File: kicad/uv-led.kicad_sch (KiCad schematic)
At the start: 11 parts, among them J1 JST_PH_B2B-PH-K_1x02_P2.00mm_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

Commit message: added screw specs to silkscreen (#3)
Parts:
- H1, H2: footprint MountingHole:MountingHole_3.2mm_M3_DIN965_Pad_TopOnly -> MountingHole:MountingHole_3.2mm_M3_ISO14580_Pad_TopOnly
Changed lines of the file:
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@@
 		)
 		(instances
-			(project "uv-led-pcb"
+			(project "uv-led"
 				(path "/e67fac83-14c9-457c-9fba-69cbeffeeea3"
 					(reference "#FLG03")
@@
 			)
 		)
-		(property "Footprint" "MountingHole:MountingHole_3.2mm_M3_DIN965_Pad_TopOnly"
+		(property "Footprint" "MountingHole:MountingHole_3.2mm_M3_ISO14580_Pad_TopOnly"
 			(at 152.4 102.87 0)
 			(hide yes)
@@
 		)
 		(instances
-			(project "uv-led-pcb"
+			(project "uv-led"
 				(path "/e67fac83-14c9-457c-9fba-69cbeffeeea3"
 					(reference "H1")
@@
 		)
 		(instances
-			(project "uv-led-pcb"
+			(project "uv-led"
 				(path "/e67fac83-14c9-457c-9fba-69cbeffeeea3"
 					(reference "D3")
@@
 		)
 		(instances
-			(project "uv-led-pcb"
+			(project "uv-led"
 				(path "/e67fac83-14c9-457c-9fba-69cbeffeeea3"
 					(reference "D2")
@@
 		)
 		(instances
-			(project "uv-led-pcb"
+			(project "uv-led"
 				(path "/e67fac83-14c9-457c-9fba-69cbeffeeea3"
 					(reference "D4")
@@
 		)
 		(instances
-			(project "uv-led-pcb"
+			(project "uv-led"
 				(path "/e67fac83-14c9-457c-9fba-69cbeffeeea3"
 					(reference "#PWR08")
@@
 		)
 		(instances
-			(project "uv-led-pcb"
+			(project "uv-led"
 				(path "/e67fac83-14c9-457c-9fba-69cbeffeeea3"
 					(reference "#PWR04")
@@
 		)
 		(instances
-			(project "uv-led-pcb"
+			(project "uv-led"
 				(path "/e67fac83-14c9-457c-9fba-69cbeffeeea3"
 					(reference "J1")
@@
 		)
 		(instances
-			(project "uv-led-pcb"
+			(project "uv-led"
 				(path "/e67fac83-14c9-457c-9fba-69cbeffeeea3"
 					(reference "#FLG04")
@@
 			)
 		)
-		(property "Footprint" "MountingHole:MountingHole_3.2mm_M3_DIN965_Pad_TopOnly"
+		(property "Footprint" "MountingHole:MountingHole_3.2mm_M3_ISO14580_Pad_TopOnly"
 			(at 177.8 102.87 0)
 			(hide yes)
@@
 		)
 		(instances
-			(project "uv-led-pcb"
+			(project "uv-led"
 				(path "/e67fac83-14c9-457c-9fba-69cbeffeeea3"
 					(reference "H2")
@@
 		)
 		(instances
-			(project "uv-led-pcb"
+			(project "uv-led"
 				(path "/e67fac83-14c9-457c-9fba-69cbeffeeea3"
 					(reference "D1")
@@
 		)
 		(instances
-			(project "uv-led-pcb"
+			(project "uv-led"
 				(path "/e67fac83-14c9-457c-9fba-69cbeffeeea3"
 					(reference "#PWR07")
@@
 		)
 		(instances
-			(project "uv-led-pcb"
+			(project "uv-led"
 				(path "/e67fac83-14c9-457c-9fba-69cbeffeeea3"
 					(reference "D5")
@@
 		)
 		(instances
-			(project "uv-led-pcb"
+			(project "uv-led"
 				(path "/e67fac83-14c9-457c-9fba-69cbeffeeea3"
 					(reference "#PWR02")
@@
 		)
 		(instances
-			(project "uv-led-pcb"
+			(project "uv-led"
 				(path "/e67fac83-14c9-457c-9fba-69cbeffeeea3"
 					(reference "#PWR03")
@@
 		)
 		(instances
-			(project "uv-led-pcb"
+			(project "uv-led"
 				(path "/e67fac83-14c9-457c-9fba-69cbeffeeea3"
 					(reference "H3")
@@
 		)
 		(instances
-			(project "uv-led-pcb"
+			(project "uv-led"
 				(path "/e67fac83-14c9-457c-9fba-69cbeffeeea3"
 					(reference "R1")
@@
 		)
 		(instances
-			(project "uv-led-pcb"
+			(project "uv-led"
 				(path "/e67fac83-14c9-457c-9fba-69cbeffeeea3"
 					(reference "H4")
@@
 		)
 		(instances
-			(project "uv-led-pcb"
+			(project "uv-led"
 				(path "/e67fac83-14c9-457c-9fba-69cbeffeeea3"
 					(reference "#PWR01")

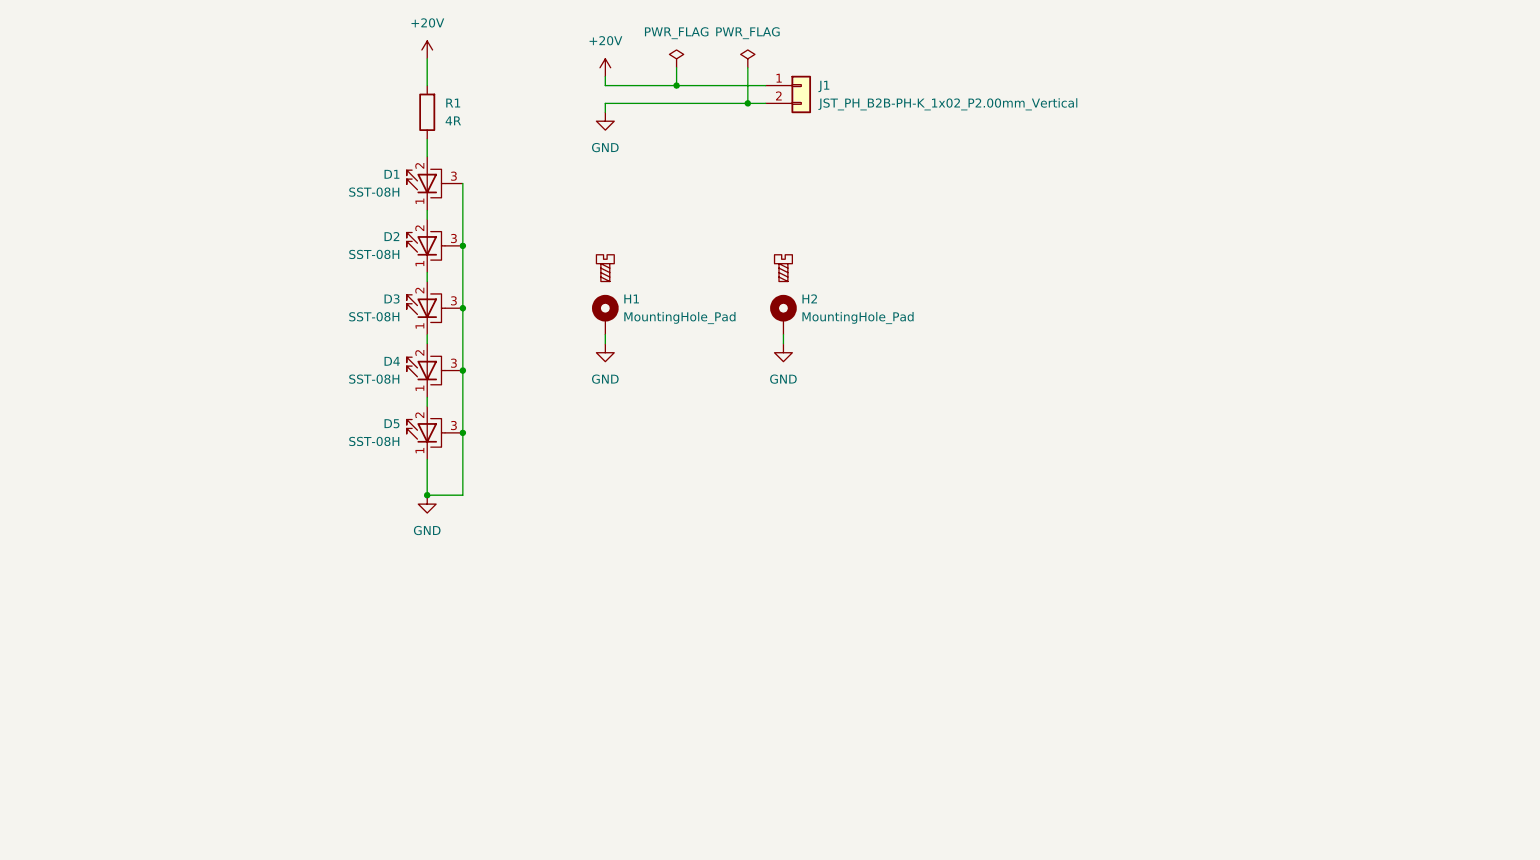
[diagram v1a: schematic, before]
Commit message: added design infos to PCB and schematic (#11)
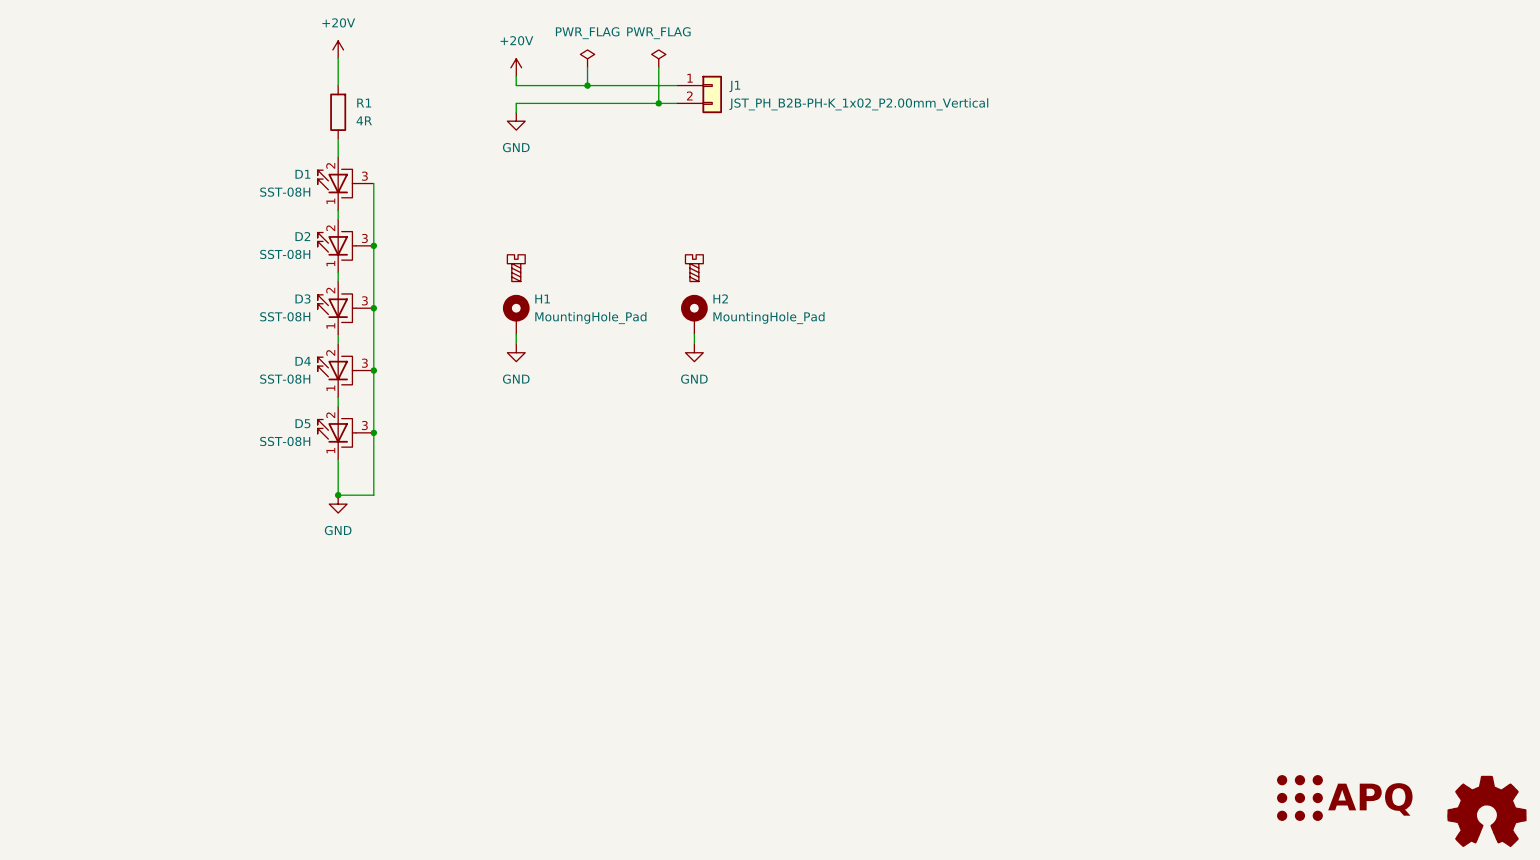
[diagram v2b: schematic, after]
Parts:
- added LOGO1: Logo_APQ, Custom_footprints_project:APQ-Logo_small, symbol Custom_logos:Logo_APQ
- added LOGO3: Logo_Open_Hardware_Small, Symbol:OSHW-Logo_7.5x8mm_SilkScreen, symbol Graphic:Logo_Open_Hardware_Small
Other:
- company: APQ - TU Darmstadt -> TU Darmstadt
- title: UV LED PCB -> QUIPS-C UV-LED
- moved on the sheet: D1, D2, D3, D4, D5, H1, H2, J1, R1

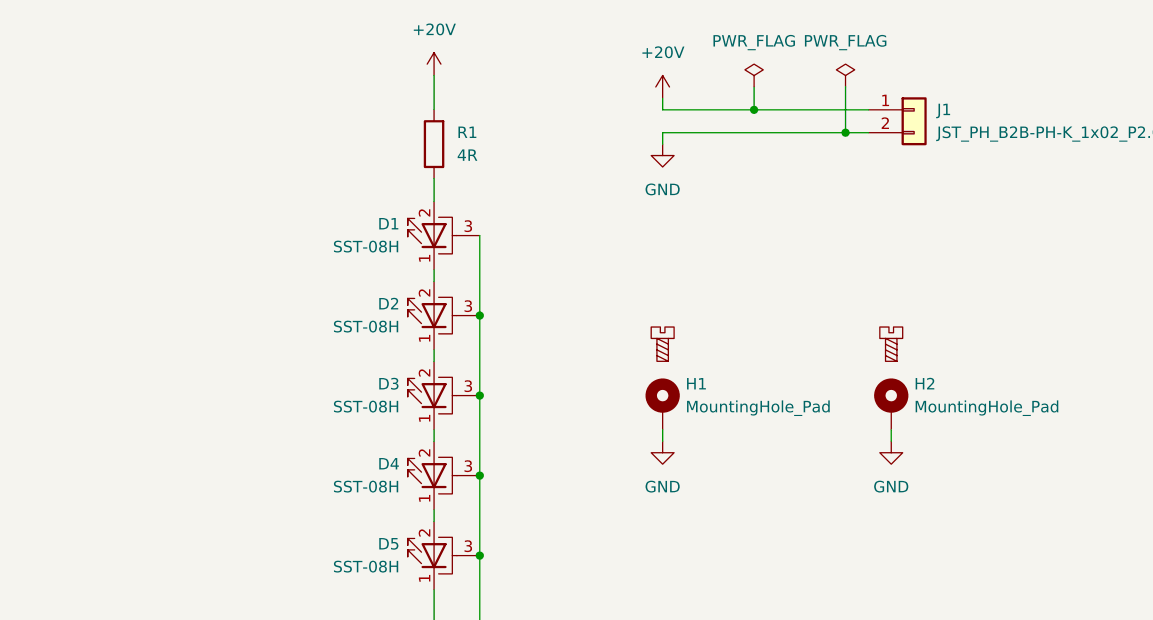
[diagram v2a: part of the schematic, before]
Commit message: added power and electrical details to schematic, updated silkscreen on PCB (#10)
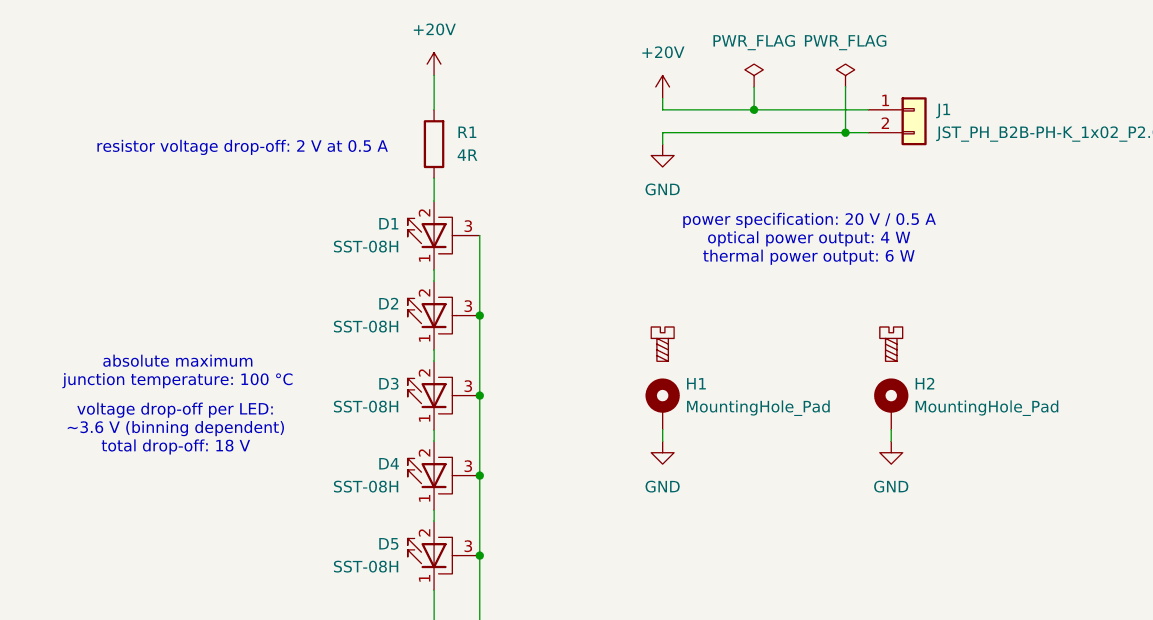
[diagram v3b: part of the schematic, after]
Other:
- note added: "absolute maximum junction temperature: 100 °C"
- note added: "power specification: 20 V / 0.5 A optical power output: 4 W thermal power output: 6 W"
- note added: "resistor voltage drop-off: 2 V at 0.5 A"
- note added: "voltage drop-off per LED: ~3.6 V (binning dependent) total drop-off: 18 V"
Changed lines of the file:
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@@
 		(comment 2 "Licensed under CERN OHL-W v2.0")
+	)
+	(text "absolute maximum\njunction temperature: 100 °C"
+		(exclude_from_sim no)
+		(at 85.852 99.06 0)
+		(effects
+			(font
+				(size 1.27 1.27)
+			)
+		)
+	)
+	(text "voltage drop-off per LED:\n~3.6 V (binning dependent)\ntotal drop-off: 18 V"
+		(exclude_from_sim no)
+		(at 85.598 105.41 0)
+		(effects
+			(font
+				(size 1.27 1.27)
+			)
+		)
+	)
+	(text "resistor voltage drop-off: 2 V at 0.5 A"
+		(exclude_from_sim no)
+		(at 92.964 74.168 0)
+		(effects
+			(font
+				(size 1.27 1.27)
+			)
+		)
+	)
+	(text "power specification: 20 V / 0.5 A\noptical power output: 4 W\nthermal power output: 6 W"
+		(exclude_from_sim no)
+		(at 155.956 84.328 0)
+		(effects
+			(font
+				(size 1.27 1.27)
+			)
+		)
 	)
 	(junction

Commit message: added operating temperatures and RoHs compliance of resistor and LEDs (#13)
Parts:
- D1: RoHS (none) -> Yes; Temperature (none) -> Top = 0 °C to 125 °C
- D2, D3, D4, D5: RoHS (none) -> Yes; Temperature (none) -> Top = 0 °C to 100 °C
- R1: RoHS (none) -> By exemption; Temperature (none) -> Top = -55 °C to 100 °C
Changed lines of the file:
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@@
+			)
+		)
+		(property "Temperature" "Top = 0 °C to 100 °C"
+			(at 114.3 101.6 90)
+			(hide yes)
+			(show_name no)
+			(do_not_autoplace no)
+			(effects
+				(font
+					(size 1.27 1.27)
+				)
+			)
+		)
+		(property "RoHS" "Yes"
+			(at 114.3 101.6 90)
+			(hide yes)
+			(show_name no)
+			(do_not_autoplace no)
+			(effects
+				(font
+					(size 1.27 1.27)
+				)
 			)
 		)
@@
 			)
 		)
+		(property "Temperature" "Top = 0 °C to 100 °C"
+			(at 114.3 92.71 90)
+			(hide yes)
+			(show_name no)
+			(do_not_autoplace no)
+			(effects
+				(font
+					(size 1.27 1.27)
+				)
+			)
+		)
+		(property "RoHS" "Yes"
+			(at 114.3 92.71 90)
+			(hide yes)
+			(show_name no)
+			(do_not_autoplace no)
+			(effects
+				(font
+					(size 1.27 1.27)
+				)
+			)
+		)
 		(pin "3"
 		)
@@
 			)
 		)
+		(property "Temperature" "Top = 0 °C to 100 °C"
+			(at 114.3 110.49 90)
+			(hide yes)
+			(show_name no)
+			(do_not_autoplace no)
+			(effects
+				(font
+					(size 1.27 1.27)
+				)
+			)
+		)
+		(property "RoHS" "Yes"
+			(at 114.3 110.49 90)
+			(hide yes)
+			(show_name no)
+			(do_not_autoplace no)
+			(effects
+				(font
+					(size 1.27 1.27)
+				)
+			)
+		)
 		(pin "3"
 		)
@@
 			)
 		)
+		(property "Temperature" "Top = 0 °C to 125 °C"
+			(at 114.3 83.82 90)
+			(hide yes)
+			(show_name no)
+			(do_not_autoplace no)
+			(effects
+				(font
+					(size 1.27 1.27)
+				)
+			)
+		)
+		(property "RoHS" "Yes"
+			(at 114.3 83.82 90)
+			(hide yes)
+			(show_name no)
+			(do_not_autoplace no)
+			(effects
+				(font
+					(size 1.27 1.27)
+				)
+			)
+		)
 		(pin "3"
 		)
@@
 			)
 		)
+		(property "Temperature" "Top = 0 °C to 100 °C"
+			(at 114.3 119.38 90)
+			(hide yes)
+			(show_name no)
+			(do_not_autoplace no)
+			(effects
+				(font
+					(size 1.27 1.27)
+				)
+			)
+		)
+		(property "RoHS" "Yes"
+			(at 114.3 119.38 90)
+			(hide yes)
+			(show_name no)
+			(do_not_autoplace no)
+			(effects
+				(font
+					(size 1.27 1.27)
+				)
+			)
+		)
 		(pin "3"
 		)
@@
 			(hide yes)
 			(show_name no)
+			(do_not_autoplace no)
+			(effects
+				(font
+					(size 1.27 1.27)
+				)
+			)
+		)
+		(property "Temperature" "Top = -55 °C to 100 °C"
+			(at 114.3 73.66 0)
+			(hide yes)
+			(show_name no)
+			(do_not_autoplace no)
+			(effects
+				(font
+					(size 1.27 1.27)
+				)
+			)
+		)
+		(property "RoHS" "By exemption"
+			(at 114.3 73.66 0)
+			(hide yes)
+			(show_name no)
